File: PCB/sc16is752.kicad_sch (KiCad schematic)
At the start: 30 parts, among them IC12 SN74LVC1G125DBVT, U1 SC16IS752IPW_128, U2 SC16IS752IPW_128, U3 CD74HC138QM96Q1, U4 SC16IS752IPW_128, U5 SC16IS752IPW_128, U6 SC16IS752IPW_128, U7 SC16IS752IPW_128

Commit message: Capacitor placement
Moved some decoupling caps from the top to the bottom. Also, file organization
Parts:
- added C46, C47: 0.1uF, Capacitor_SMD:C_0805_2012Metric_Pad1.18x1.45mm_HandSolder, symbol Device:C
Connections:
- net +3V3: now also C46.2, C47.2
- net GND: now also C46.1, C47.1
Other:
- note added: "Spare Decoupling Capacitors"

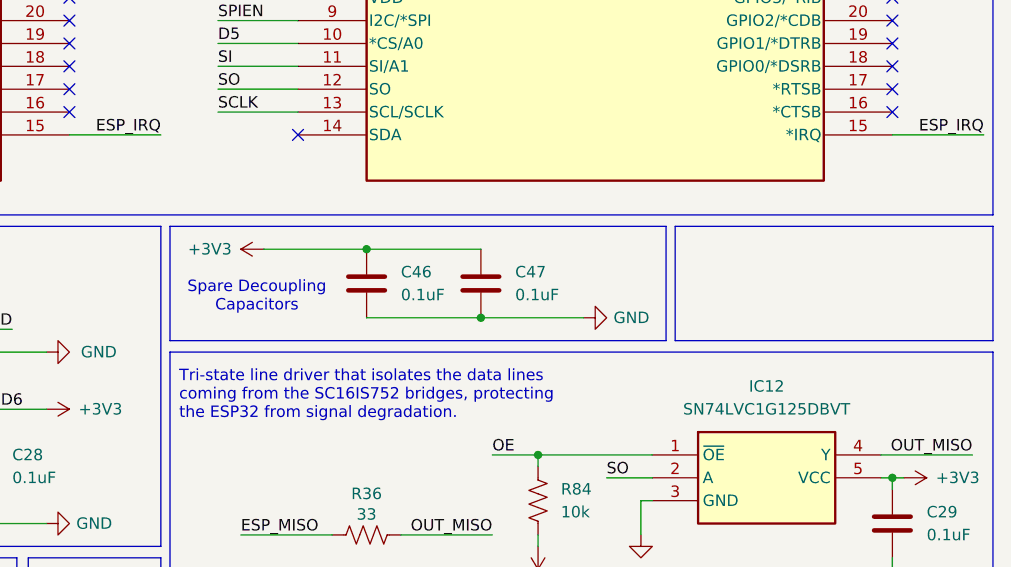
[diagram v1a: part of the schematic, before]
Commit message: Add footprints & datasheets; clean PCB file
Add numerous component datasheets to PCB/Datasheets and introduce new footprints (DarkMagic:SRN2010BTA3R3M and DarkMagic:1812L010DR). Remove many redundant KiLib_Generator properties and perform footprint edits across the board including placement/rotation changes, pad orientation/net fixes, value and UUID updates, and silkscreen/fab text adjustments. Also add KiCad editor lock files (~DarkMagic.kicad_pcb.lck, ~DarkMagic.kicad_sch.lck).
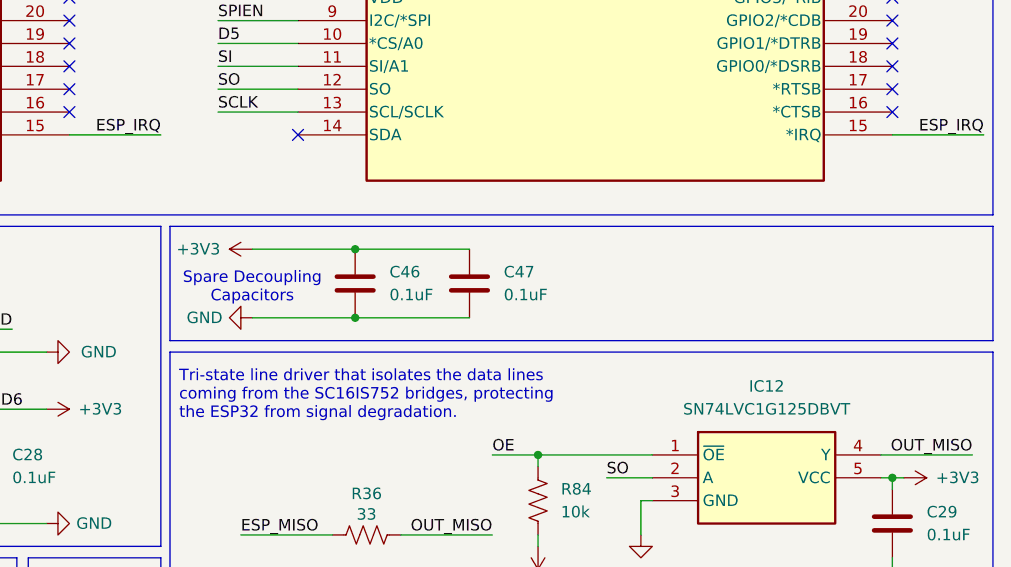
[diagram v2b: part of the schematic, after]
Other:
- moved on the sheet: C46, C47
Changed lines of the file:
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@@
 	(rectangle
 		(start 192.786 121.92)
-		(end 247.904 134.62)
+		(end 284.226 134.62)
 		(stroke
 			(width 0)
@@
 	)
 	(rectangle
-		(start 248.92 121.92)
-		(end 284.226 134.62)
-		(stroke
-			(width 0)
-			(type default)
-			(color 0 0 0 1)
-		)
-		(fill
-			(type cross_hatch)
-			(color 0 0 0 1)
-		)
-	)
-	(rectangle
 		(start 192.786 135.89)
 		(end 284.226 165.1)
@@
 	(text "Spare Decoupling\nCapacitors"
 		(exclude_from_sim no)
-		(at 202.438 129.794 0)
+		(at 201.93 128.778 0)
 		(effects
 			(font
@@
 	)
 	(junction
-		(at 171.45 135.89)
+		(at 213.36 132.08)
 		(diameter 0)
 		(color 0 0 0 0)
 	)
 	(junction
-		(at 227.33 132.08)
+		(at 171.45 135.89)
 		(diameter 0)
 		(color 0 0 0 0)
@@
 	)
 	(junction
-		(at 214.63 124.46)
+		(at 213.36 124.46)
 		(diameter 0)
 		(color 0 0 0 0)
@@
 	(wire
 		(pts
+			(xy 213.36 132.08) (xy 226.06 132.08)
+		)
+		(stroke
+			(width 0)
+			(type default)
+		)
+	)
+	(wire
+		(pts
 			(xy 149.86 175.26) (xy 149.86 180.34)
 		)
@@
 	(wire
 		(pts
-			(xy 214.63 132.08) (xy 227.33 132.08)
-		)
-		(stroke
-			(width 0)
-			(type default)
-		)
-	)
-	(wire
-		(pts
 			(xy 90.17 38.1) (xy 96.52 38.1)
 		)
@@
 	(wire
 		(pts
-			(xy 227.33 132.08) (xy 238.76 132.08)
+			(xy 201.93 132.08) (xy 213.36 132.08)
 		)
 		(stroke
@@
 	(wire
 		(pts
-			(xy 203.2 124.46) (xy 214.63 124.46)
+			(xy 201.93 124.46) (xy 213.36 124.46)
 		)
 		(stroke
@@
 	(wire
 		(pts
-			(xy 214.63 124.46) (xy 227.33 124.46)
+			(xy 213.36 124.46) (xy 226.06 124.46)
 		)
 		(stroke
@@
 	(symbol
 		(lib_id "power:+3V3")
-		(at 203.2 124.46 90)
+		(at 201.93 124.46 90)
 		(unit 1)
 		(body_style 1)
@@
 		(dnp no)
 		(property "Reference" "#PWR079"
-			(at 207.01 124.46 0)
+			(at 205.74 124.46 0)
 			(hide yes)
 			(show_name no)
@@
 		)
 		(property "Value" "+3V3"
-			(at 199.644 124.46 90)
+			(at 198.374 124.46 90)
 			(show_name no)
 			(do_not_autoplace no)
@@
 		)
 		(property "Footprint" ""
-			(at 203.2 124.46 0)
+			(at 201.93 124.46 0)
 			(hide yes)
 			(show_name no)
@@
 		)
 		(property "Datasheet" ""
-			(at 203.2 124.46 0)
+			(at 201.93 124.46 0)
 			(hide yes)
 			(show_name no)
@@
 		)
 		(property "Description" "Power symbol creates a global label with name \"+3V3\""
-			(at 203.2 124.46 0)
+			(at 201.93 124.46 0)
 			(hide yes)
 			(show_name no)
@@
 	(symbol
 		(lib_id "Device:C")
-		(at 227.33 128.27 180)
+		(at 226.06 128.27 180)
 		(unit 1)
 		(body_style 1)
@@
 		(dnp no)
 		(property "Reference" "C47"
-			(at 231.14 126.9999 0)
+			(at 229.87 126.9999 0)
 			(show_name no)
 			(do_not_autoplace no)
@@
 		)
 		(property "Value" "0.1uF"
-			(at 231.14 129.5399 0)
+			(at 229.87 129.5399 0)
 			(show_name no)
 			(do_not_autoplace no)
@@
 		)
 		(property "Footprint" "Capacitor_SMD:C_0805_2012Metric_Pad1.18x1.45mm_HandSolder"
-			(at 226.3648 124.46 0)
+			(at 225.0948 124.46 0)
 			(hide yes)
 			(show_name no)
@@
 		)
 		(property "Datasheet" ""
-			(at 227.33 128.27 0)
+			(at 226.06 128.27 0)
 			(hide yes)
 			(show_name no)
@@
 		)
 		(property "Description" "Unpolarized capacitor"
-			(at 227.33 128.27 0)
+			(at 226.06 128.27 0)
 			(hide yes)
 			(show_name no)
@@
 		)
 		(property "Manufacturer_Part_Number" "CL21B104KCC5PNC "
-			(at 227.33 128.27 0)
+			(at 226.06 128.27 0)
 			(hide yes)
 			(show_name no)
@@
 		)
 		(property "Mouser Part Number" "187-CL21B104KCC5PNC "
-			(at 227.33 128.27 0)
+			(at 226.06 128.27 0)
 			(hide yes)
 			(show_name no)
@@
 		)
 		(property "Maunfacturer Part Number" ""
-			(at 227.33 128.27 0)
+			(at 226.06 128.27 0)
 			(hide yes)
 			(show_name no)
@@
 		)
 		(property "AVAILABILITY" ""
-			(at 227.33 128.27 0)
+			(at 226.06 128.27 0)
 			(hide yes)
 			(show_name no)
@@
 		)
 		(property "Check_prices" ""
-			(at 227.33 128.27 0)
+			(at 226.06 128.27 0)
 			(hide yes)
 			(show_name no)
@@
 		)
 		(property "MF" ""
-			(at 227.33 128.27 0)
+			(at 226.06 128.27 0)
 			(hide yes)
 			(show_name no)
@@
 		)
 		(property "MP" ""
-			(at 227.33 128.27 0)
+			(at 226.06 128.27 0)
 			(hide yes)
 			(show_name no)
@@
 		)
 		(property "Maunfacturer_Part_Number" ""
-			(at 227.33 128.27 0)
+			(at 226.06 128.27 0)
 			(hide yes)
 			(show_name no)
@@
 		)
 		(property "PACKAGE" ""
-			(at 227.33 128.27 0)
+			(at 226.06 128.27 0)
 			(hide yes)
 			(show_name no)
@@
 		)
 		(property "PARTREV" ""
-			(at 227.33 128.27 0)
+			(at 226.06 128.27 0)
 			(hide yes)
 			(show_name no)
@@
 		)
 		(property "PRICE" ""
-			(at 227.33 128.27 0)
+			(at 226.06 128.27 0)
 			(hide yes)
 			(show_name no)
@@
 		)
 		(property "STANDARD" ""
-			(at 227.33 128.27 0)
+			(at 226.06 128.27 0)
 			(hide yes)
 			(show_name no)
@@
 		)
 		(property "SnapEDA_Link" ""
-			(at 227.33 128.27 0)
+			(at 226.06 128.27 0)
 			(hide yes)
 			(show_name no)
@@
 	(symbol
 		(lib_id "power:GND")
-		(at 238.76 132.08 90)
+		(at 201.93 132.08 270)
 		(unit 1)
 		(body_style 1)
@@
 		(dnp no)
 		(property "Reference" "#PWR030"
-			(at 245.11 132.08 0)
+			(at 195.58 132.08 0)
 			(hide yes)
 			(show_name no)
@@
 		)
 		(property "Value" "GND"
-			(at 242.062 132.08 90)
+			(at 198.628 132.08 90)
 			(show_name no)
 			(do_not_autoplace no)
@@
 		)
 		(property "Footprint" ""
-			(at 238.76 132.08 0)
+			(at 201.93 132.08 0)
 			(hide yes)
 			(show_name no)
@@
 		)
 		(property "Datasheet" ""
-			(at 238.76 132.08 0)
+			(at 201.93 132.08 0)
 			(hide yes)
 			(show_name no)
@@
 		)
 		(property "Description" "Power symbol creates a global label with name \"GND\" , ground"
-			(at 238.76 132.08 0)
+			(at 201.93 132.08 0)
 			(hide yes)
 			(show_name no)
@@
 	(symbol
 		(lib_id "Device:C")
-		(at 214.63 128.27 180)
+		(at 213.36 128.27 180)
 		(unit 1)
 		(body_style 1)
@@
 		(dnp no)
 		(property "Reference" "C46"
-			(at 218.44 126.9999 0)
+			(at 217.17 126.9999 0)
 			(show_name no)
 			(do_not_autoplace no)
@@
 		)
 		(property "Value" "0.1uF"
-			(at 218.44 129.5399 0)
+			(at 217.17 129.5399 0)
 			(show_name no)
 			(do_not_autoplace no)
@@
 		)
 		(property "Footprint" "Capacitor_SMD:C_0805_2012Metric_Pad1.18x1.45mm_HandSolder"
-			(at 213.6648 124.46 0)
+			(at 212.3948 124.46 0)
 			(hide yes)
 			(show_name no)
@@
 		)
 		(property "Datasheet" ""
-			(at 214.63 128.27 0)
+			(at 213.36 128.27 0)
 			(hide yes)
 			(show_name no)
@@
 		)
 		(property "Description" "Unpolarized capacitor"
-			(at 214.63 128.27 0)
+			(at 213.36 128.27 0)
 			(hide yes)
 			(show_name no)
@@
 		)
 		(property "Manufacturer_Part_Number" "CL21B104KCC5PNC "
-			(at 214.63 128.27 0)
+			(at 213.36 128.27 0)
 			(hide yes)
 			(show_name no)
@@
 		)
 		(property "Mouser Part Number" "187-CL21B104KCC5PNC "
-			(at 214.63 128.27 0)
+			(at 213.36 128.27 0)
 			(hide yes)
 			(show_name no)
@@
 		)
 		(property "Maunfacturer Part Number" ""
-			(at 214.63 128.27 0)
+			(at 213.36 128.27 0)
 			(hide yes)
 			(show_name no)
@@
 		)
 		(property "AVAILABILITY" ""
-			(at 214.63 128.27 0)
+			(at 213.36 128.27 0)
 			(hide yes)
 			(show_name no)
@@
 		)
 		(property "Check_prices" ""
-			(at 214.63 128.27 0)
+			(at 213.36 128.27 0)
 			(hide yes)
 			(show_name no)
@@
 		)
 		(property "MF" ""
-			(at 214.63 128.27 0)
+			(at 213.36 128.27 0)
 			(hide yes)
 			(show_name no)
@@
 		)
 		(property "MP" ""
-			(at 214.63 128.27 0)
+			(at 213.36 128.27 0)
 			(hide yes)
 			(show_name no)
@@
 		)
 		(property "Maunfacturer_Part_Number" ""
-			(at 214.63 128.27 0)
+			(at 213.36 128.27 0)
 			(hide yes)
 			(show_name no)
@@
 		)
 		(property "PACKAGE" ""
-			(at 214.63 128.27 0)
+			(at 213.36 128.27 0)
 			(hide yes)
 			(show_name no)
@@
 		)
 		(property "PARTREV" ""
-			(at 214.63 128.27 0)
+			(at 213.36 128.27 0)
 			(hide yes)
 			(show_name no)
@@
 		)
 		(property "PRICE" ""
-			(at 214.63 128.27 0)
+			(at 213.36 128.27 0)
 			(hide yes)
 			(show_name no)
@@
 		)
 		(property "STANDARD" ""
-			(at 214.63 128.27 0)
+			(at 213.36 128.27 0)
 			(hide yes)
 			(show_name no)
@@
 		)
 		(property "SnapEDA_Link" ""
-			(at 214.63 128.27 0)
+			(at 213.36 128.27 0)
 			(hide yes)
 			(show_name no)

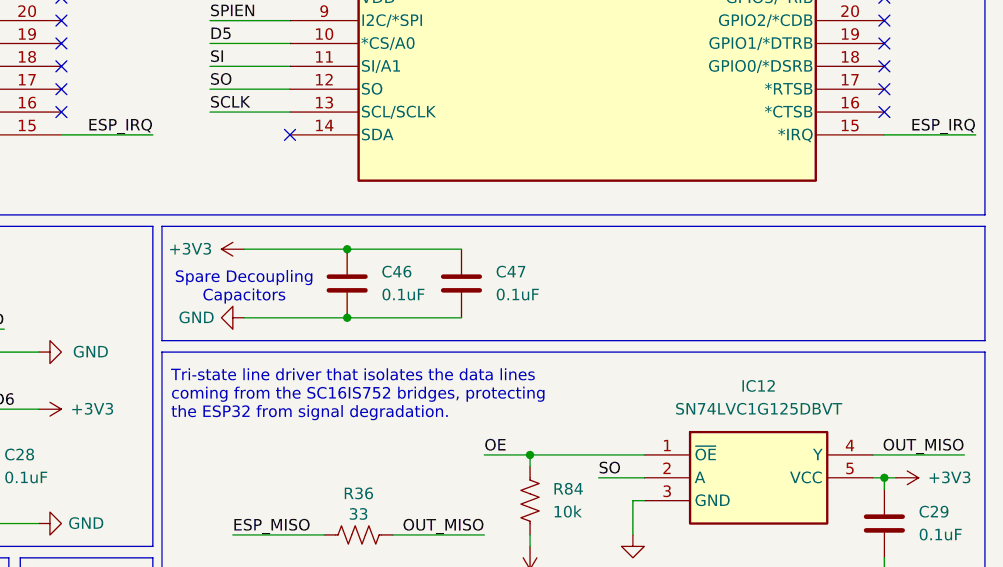
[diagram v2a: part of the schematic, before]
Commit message: Add bottom hand-solder caps and update BOM
Update PCB to add bottom-side hand-solder 0805 capacitor footprints and sync BOM. DarkMagic.csv: increment 0.1uF part count (34→35) and 4.7uF count (1→2) and update component lists. DarkMagic.kicad_pcb: add two B.Cu hand-solder capacitor footprints (C7, C10), adjust several footprint attributes (mark many SMD/TH pads as DNP or set solder_mask_margin), tweak some pad/part positions and UUIDs, and rename one net from /USB_VBUS to /CP_VBUS. Also add generated files (PCB/bom/ibom.html and PCB/database/project.db) and other production file updates to keep project metadata in sync.
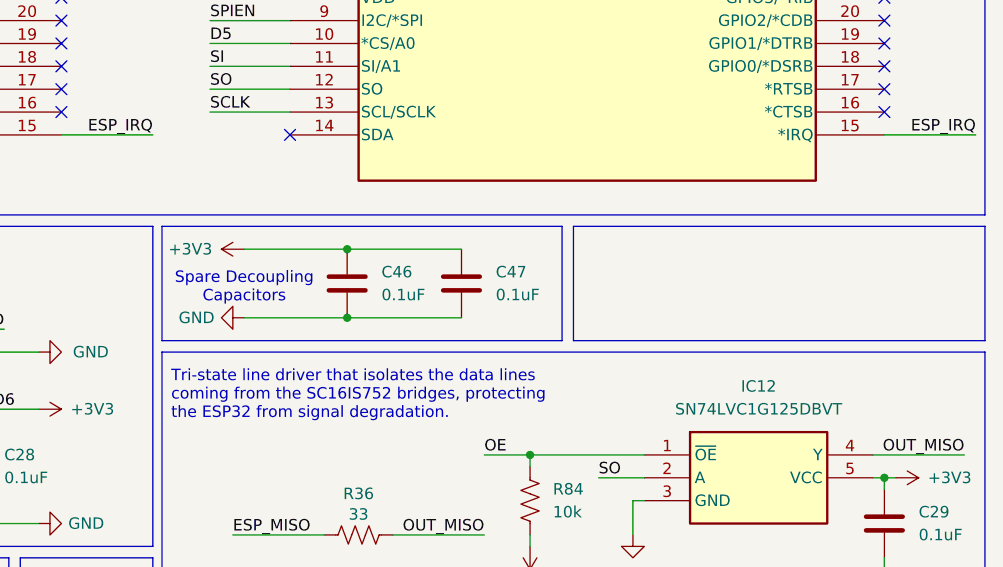
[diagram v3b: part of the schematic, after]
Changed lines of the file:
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@@
 	(rectangle
 		(start 192.786 121.92)
-		(end 284.226 134.62)
+		(end 237.236 134.62)
 		(stroke
 			(width 0)
@@
 		)
 	)
+	(rectangle
+		(start 238.506 121.92)
+		(end 284.226 134.62)
+		(stroke
+			(width 0)
+			(type solid)
+			(color 0 0 0 1)
+		)
+		(fill
+			(type cross_hatch)
+			(color 0 0 0 1)
+		)
+	)

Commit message: Add 0805 handsolder footprint and reroute nets
Add an 0805 hand-solder capacitor footprint (Pad1.18x1.45mm) on B.Cu (C50) and update existing 0805 footprint reference placement. Add copper segments and a via to connect +3V3 and GND between F.Cu and B.Cu (including new via at 148.675,37.84). Re-route several F.Cu traces (ESP_A1 and +3V3) and update segment coordinates/UUIDs. Adjust a copper zone (changed layer to F.Mask and lowered priority) and remove/replace some filled polygons. Update associated project/schematic metadata files and add schematic lock file.
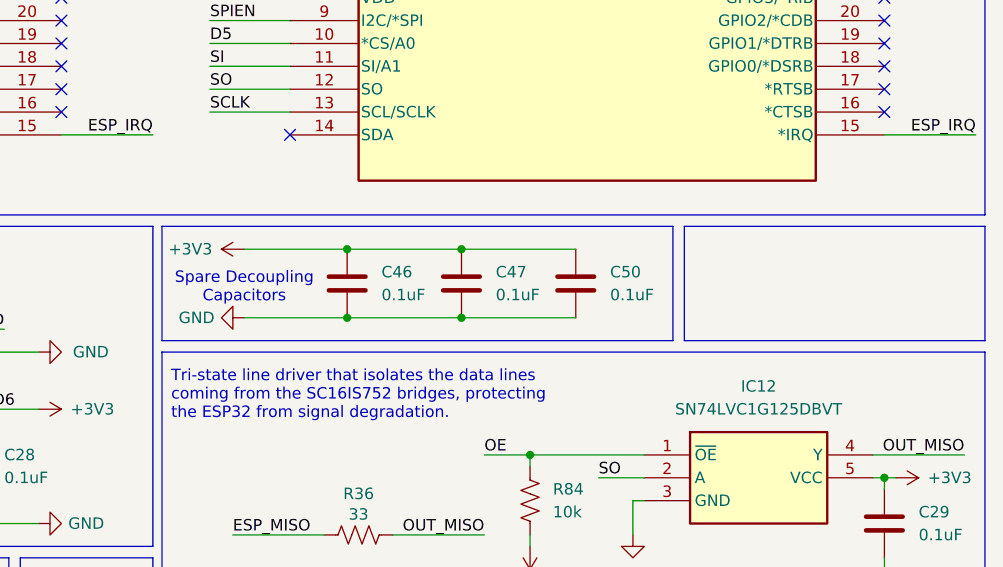
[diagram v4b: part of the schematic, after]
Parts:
- added C50: 0.1uF, Capacitor_SMD:C_0805_2012Metric_Pad1.18x1.45mm_HandSolder, symbol Device:C
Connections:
- net +3V3: now also C50.2
- net GND: now also C50.1
